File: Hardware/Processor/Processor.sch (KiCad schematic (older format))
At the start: 95 parts

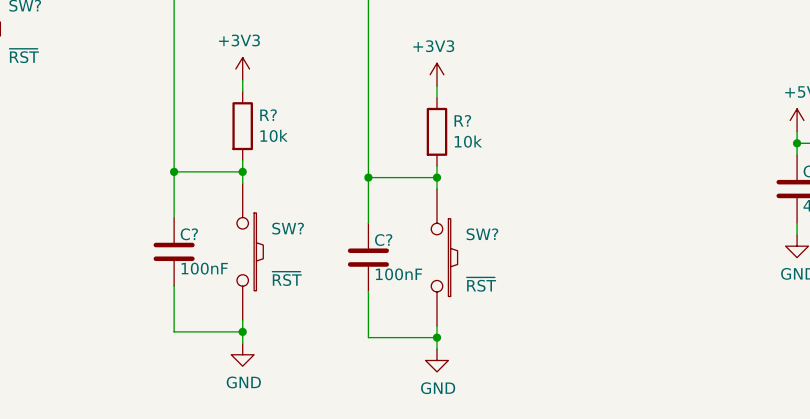
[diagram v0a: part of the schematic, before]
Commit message: Fixed names on user pushbuttons, removed color schematic
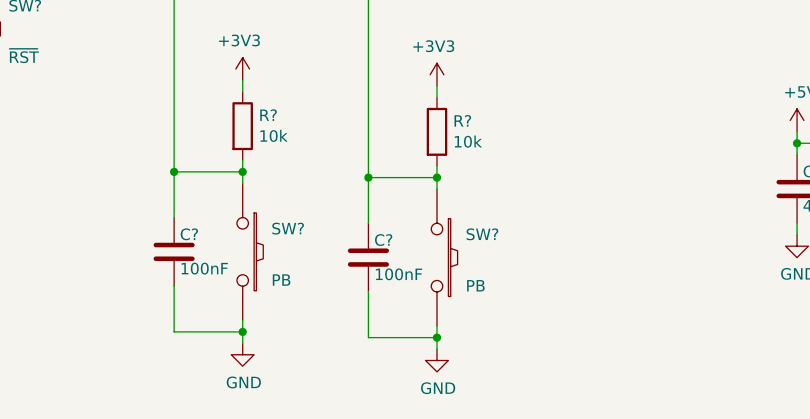
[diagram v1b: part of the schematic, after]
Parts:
- SW? (x2): value ~RST -> PB
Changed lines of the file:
@@
 P 10225 9775
 F 0 "SW?" V 10125 9900 50  0000 L CNN
-F 1 "~RST" V 10350 9900 50  0000 L CNN
+F 1 "PB" V 10350 9900 50  0000 L CNN
 F 2 "" H -225 -50 50  0000 C CNN
 F 3 "" H -225 -50 50  0000 C CNN
@@
 P 11075 9800
 F 0 "SW?" V 10975 9925 50  0000 L CNN
-F 1 "~RST" V 11200 9925 50  0000 L CNN
+F 1 "PB" V 11200 9925 50  0000 L CNN
 F 2 "" H 625 -25 50  0000 C CNN
 F 3 "" H 625 -25 50  0000 C CNN

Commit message: Added vref filter, cleaned up formatting
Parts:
- added C?: 100nF, symbol C
- TP?: value 5V -> 3V3
- TP?: value 5V -> 1V2
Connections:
- net +5V_UART: no longer J?.4 (P4), U?.7 (VCCB)
- net AREF: now also C?.1
- net GND: now also C?.2
- new net UART_5V: J?.4 (P4), U?.7 (VCCB)
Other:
- moved on the sheet: C?, J?, R?

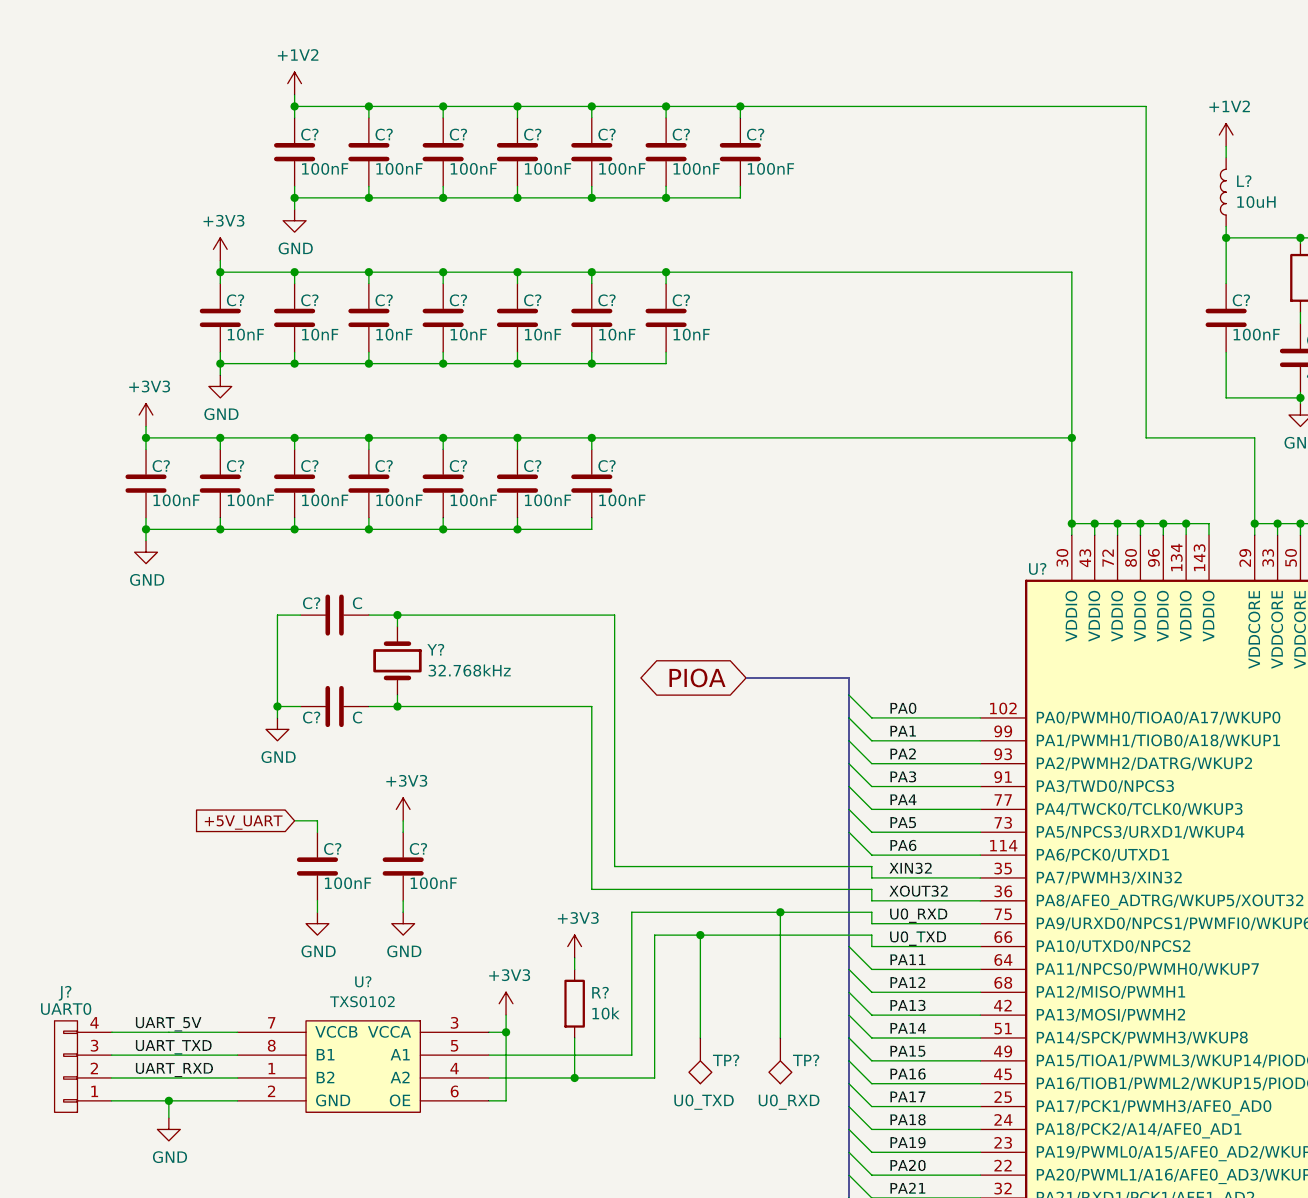
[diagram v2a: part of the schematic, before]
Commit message: Reverted 5V_UART change in last commit, regenerated PDFs
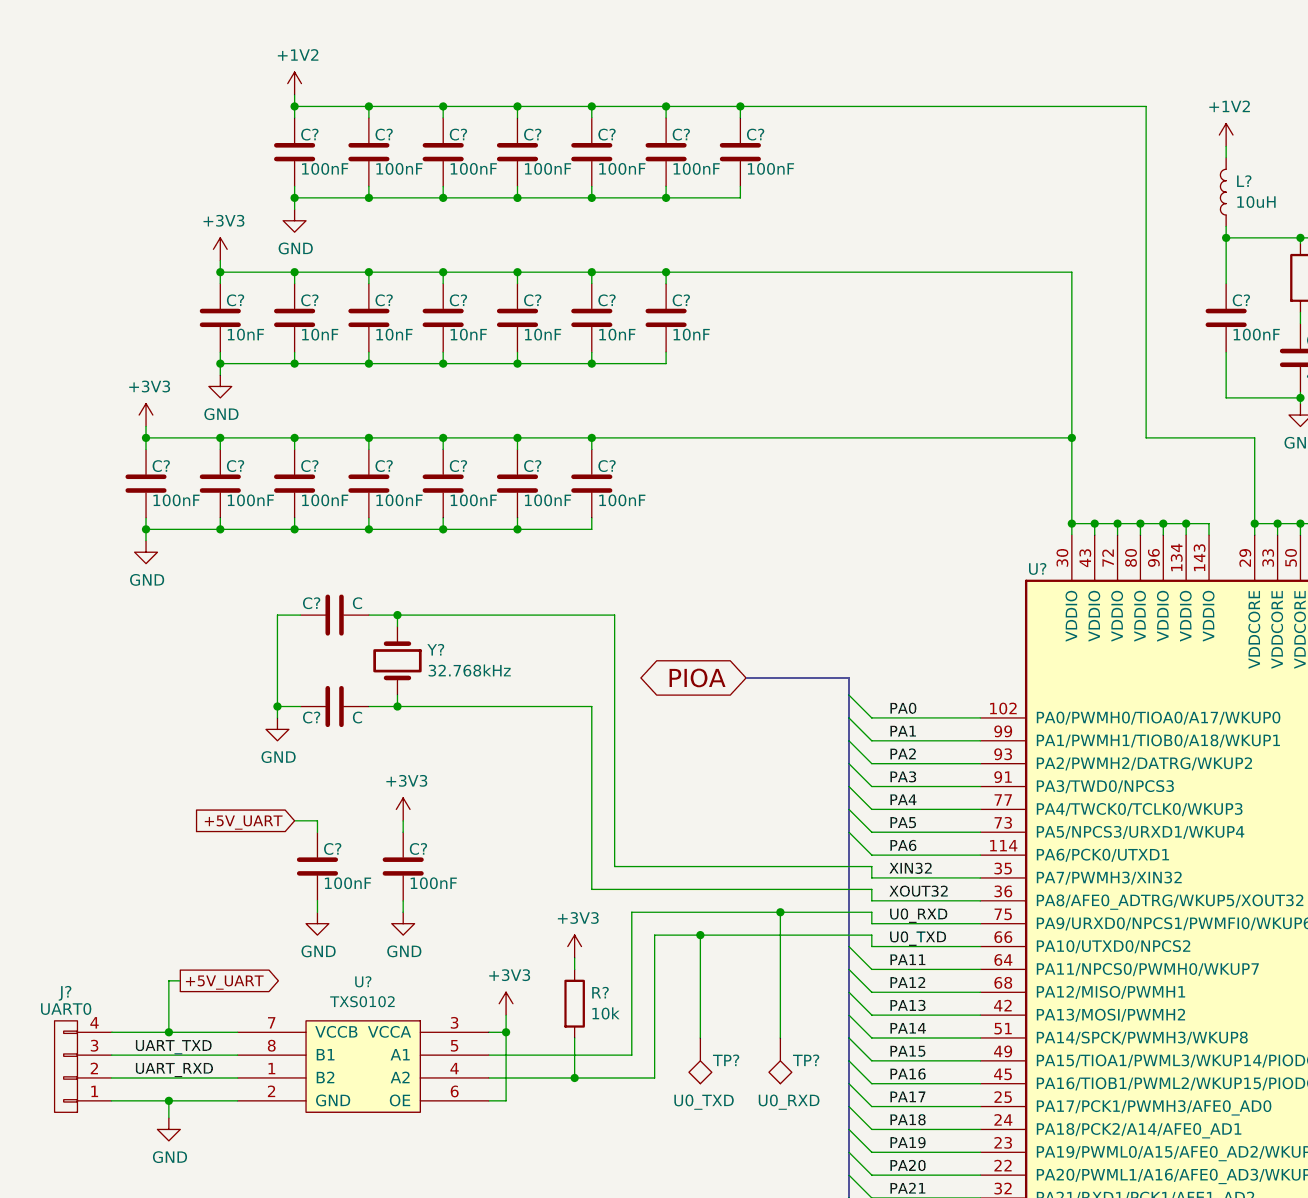
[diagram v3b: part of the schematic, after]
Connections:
- net UART_5V is gone; now on net +5V_UART: J?.4 (P4), U?.7 (VCCB)
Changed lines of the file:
@@
 	6150 2825 5675 2825
 Wire Wire Line
-	5675 2825 5675 1375
-Wire Wire Line
-	5675 1375 3900 1375
-Wire Wire Line
-	3900 1375 3575 1375
-Wire Wire Line
-	3575 1375 3250 1375
-Wire Wire Line
-	3250 1375 2925 1375
-Wire Wire Line
-	2925 1375 2600 1375
-Wire Wire Line
-	2600 1375 2275 1375
-Wire Wire Line
-	2275 1375 1950 1375
+	5675 1375 5675 2825
+Wire Wire Line
+	1950 1375 2275 1375
+Wire Wire Line
+	2275 1375 2600 1375
+Wire Wire Line
+	2600 1375 2925 1375
+Wire Wire Line
+	2925 1375 3250 1375
+Wire Wire Line
+	3250 1375 3575 1375
+Wire Wire Line
+	3575 1375 3900 1375
+Wire Wire Line
+	3900 1375 5675 1375
 Wire Wire Line
 	6950 2250 6950 3250
@@
 	10800 7225 10800 7275
 Wire Wire Line
-	4475 4950 4475 4900
-Wire Wire Line
-	4475 4900 4075 4900
-Wire Wire Line
-	4075 4900 3425 4900
+	4475 4900 4475 4950
+Wire Wire Line
+	3425 4900 4075 4900
+Wire Wire Line
+	4075 4900 4475 4900
 Wire Wire Line
 	4475 5000 4475 5050
@@
 	7875 2500 7875 3100
 Connection ~ 8450 2500
-Text Label 1250 5425 0    47   ~ 0
-UART_5V
+Text GLabel 1450 5200 2    47   Output ~ 0
++5V_UART
+Wire Wire Line
+	1450 5200 1400 5200
+Wire Wire Line
+	1400 5200 1400 5425
+Connection ~ 1400 5425
 $EndSCHEMATC

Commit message: Initial schematic annotation, regenerated PDF
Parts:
- added C36: 100nF, symbol C
- gave numbers to parts that had none: 96
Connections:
- net GND: now also C36.2
- net ~RST: now also C36.1

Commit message: Added VBUS_DETECT to USB line
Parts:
- added C?: 100nF, symbol C
- added R? (x3): 10k, symbol R
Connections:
- net GND: now also C?.2, R?.2
- net VBUS: now also C?.1, R?.2
- net PD31: no longer names the net of J8.36 (P36)
- net PD31: no longer U2.2 (PD31)
- new net: R?.1, R?.2
- new net VBUS_DET: R?.1, R?.1, U2.2 (PD31)
- no-connect marks 18 -> 19
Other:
- moved on the sheet: C8, C9, J1, JP1, Y1

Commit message: Started BOM, added refs, assigned values to sch
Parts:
- removed R8: 0R, symbol R
- added R11: 27R, symbol R
- C10: renamed from C11; value C -> 3.9pF
- C11: renamed from C12; value C -> 3.9pF
- C19: renamed from C8; value C -> 18pF
- C20: renamed from C9; value C -> 18pF
- R6: renamed from R3; value 0R -> 27R
- R7: renamed from R4; value 0R -> 27R
- U3: renamed from D1; MFG# (none) -> LM4040C30
- gave numbers to parts that had none: 4
- renumbered C13 to C12, C14 to C13, C15 to C14, C16 to C15, C17 to C16, C18 to C17, C19 to C18, C20 to C21, C21 to C22, C22 to C23, C23 to C24, C24 to C25, C25 to C26, C26 to C27, C27 to C28, C28 to C29, C29 to C30, C30 to C31, C31 to C32, C32 to C33, C33 to C35, C35 to C36, C36 to C37, C37 to C38, C38 to C39, C39 to C40, C40 to C41, C5 to C6, C6 to C7, C7 to C8, C10 to C9, D2 to D1, D3 to D2, D4 to D3, D5 to D4, D6 to D5, R7 to R10, R9 to R12, R10 to R13, R11 to R14, R12 to R15, R13 to R16, R14 to R17, R15 to R18, R16 to R19, R17 to R20, R18 to R21, R19 to R22, R2 to R5, R5 to R8, R6 to R9, SW3 to SW1, SW1 to SW3, U3 to U4, TVS1 to U5, Y2 to Y1, Y1 to Y2
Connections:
- net SWO: now also J4.3 (P3)
- net ~RST: now also R11.1; no longer C37.1
- net 5V_EXT renamed +5V_EXT
- new net: C37.1, R11.2
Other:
- moved on the sheet: C10, C11, C15, C34, C36, C9, J4, R10, R6, R7, SW3, Y1

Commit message: Fixed more KiCad sch library issues
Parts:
- U2: symbol ATSAM4E16E -> ATSAM4E16E-RESCUE-Processor
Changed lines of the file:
@@
 EESchema Schematic File Version 2
-LIBS:Processor-rescue
 LIBS:power
 LIBS:device
@@
 LIBS:valves
 LIBS:common
-LIBS:newFritzLib
 LIBS:Processor-cache
 EELAYER 26 0
@@
 $EndDescr
 $Comp
-L ATSAM4E16E U2
+L ATSAM4E16E-RESCUE-Processor U2
 U 1 1 58A11173
 P 6850 6450
